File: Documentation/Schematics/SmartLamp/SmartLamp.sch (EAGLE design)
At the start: 25 parts, among them J1 POWER_JACKPTH_BREAD, Q1 IRLZ44Z, Q2 IRLZ44Z, Q3 IRLZ44Z, U1 HM-10, U2 DS3231MZ

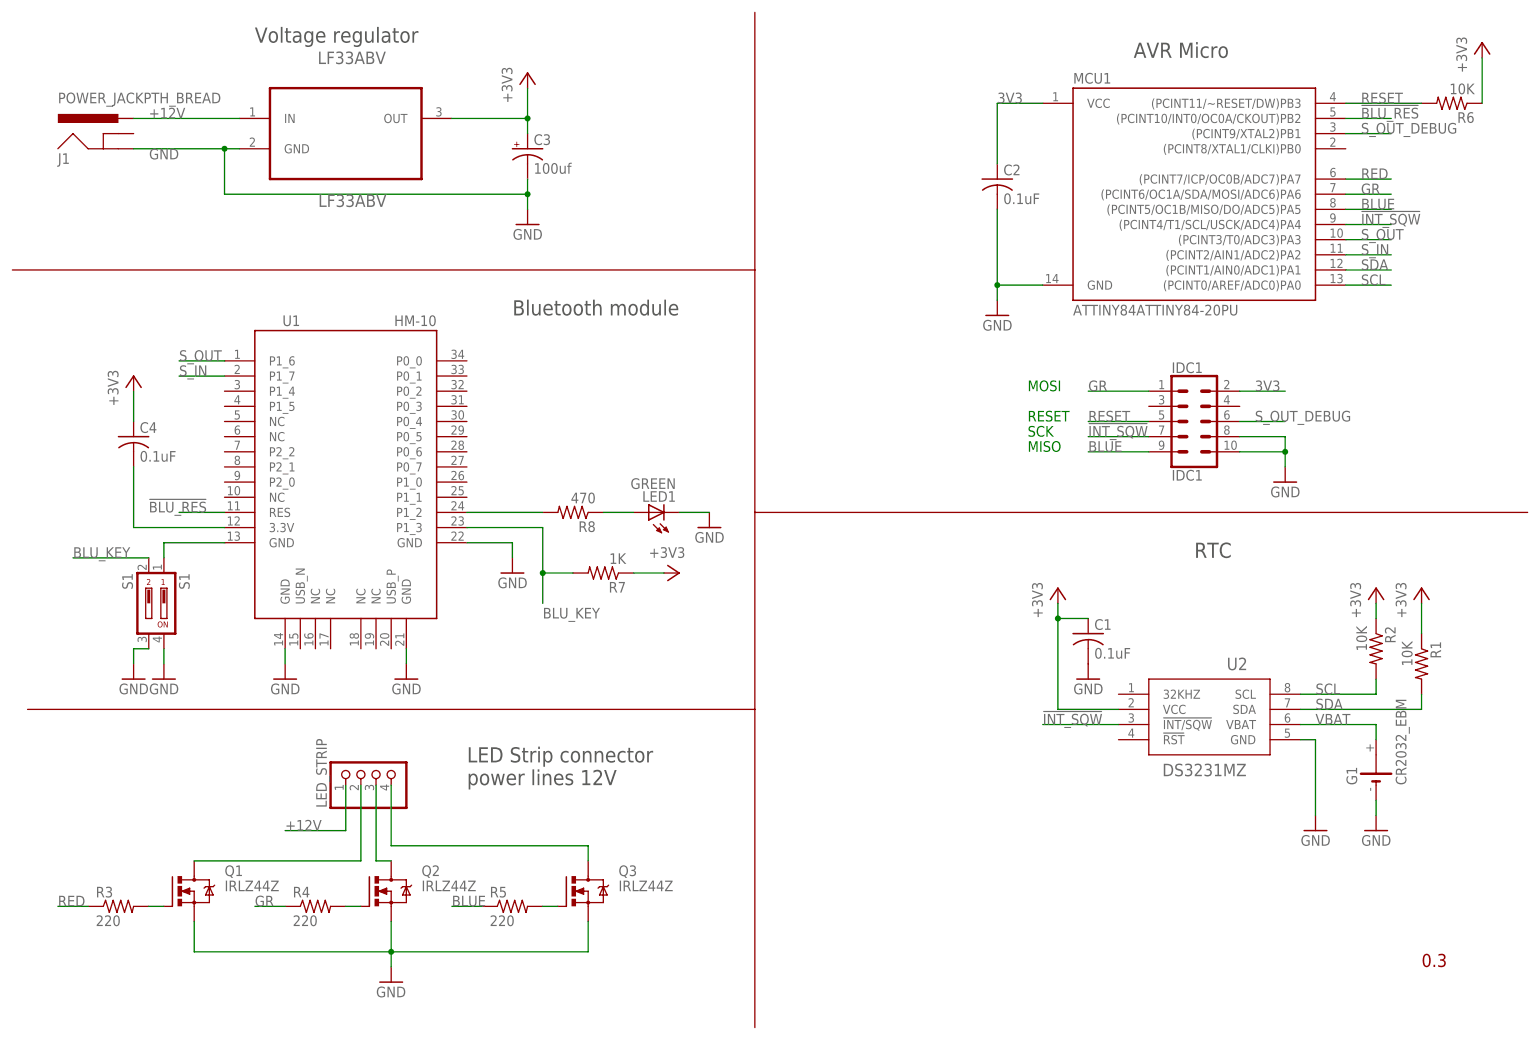
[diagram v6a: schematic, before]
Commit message: Fixed IO connections to micro, in schematic and main.cpp
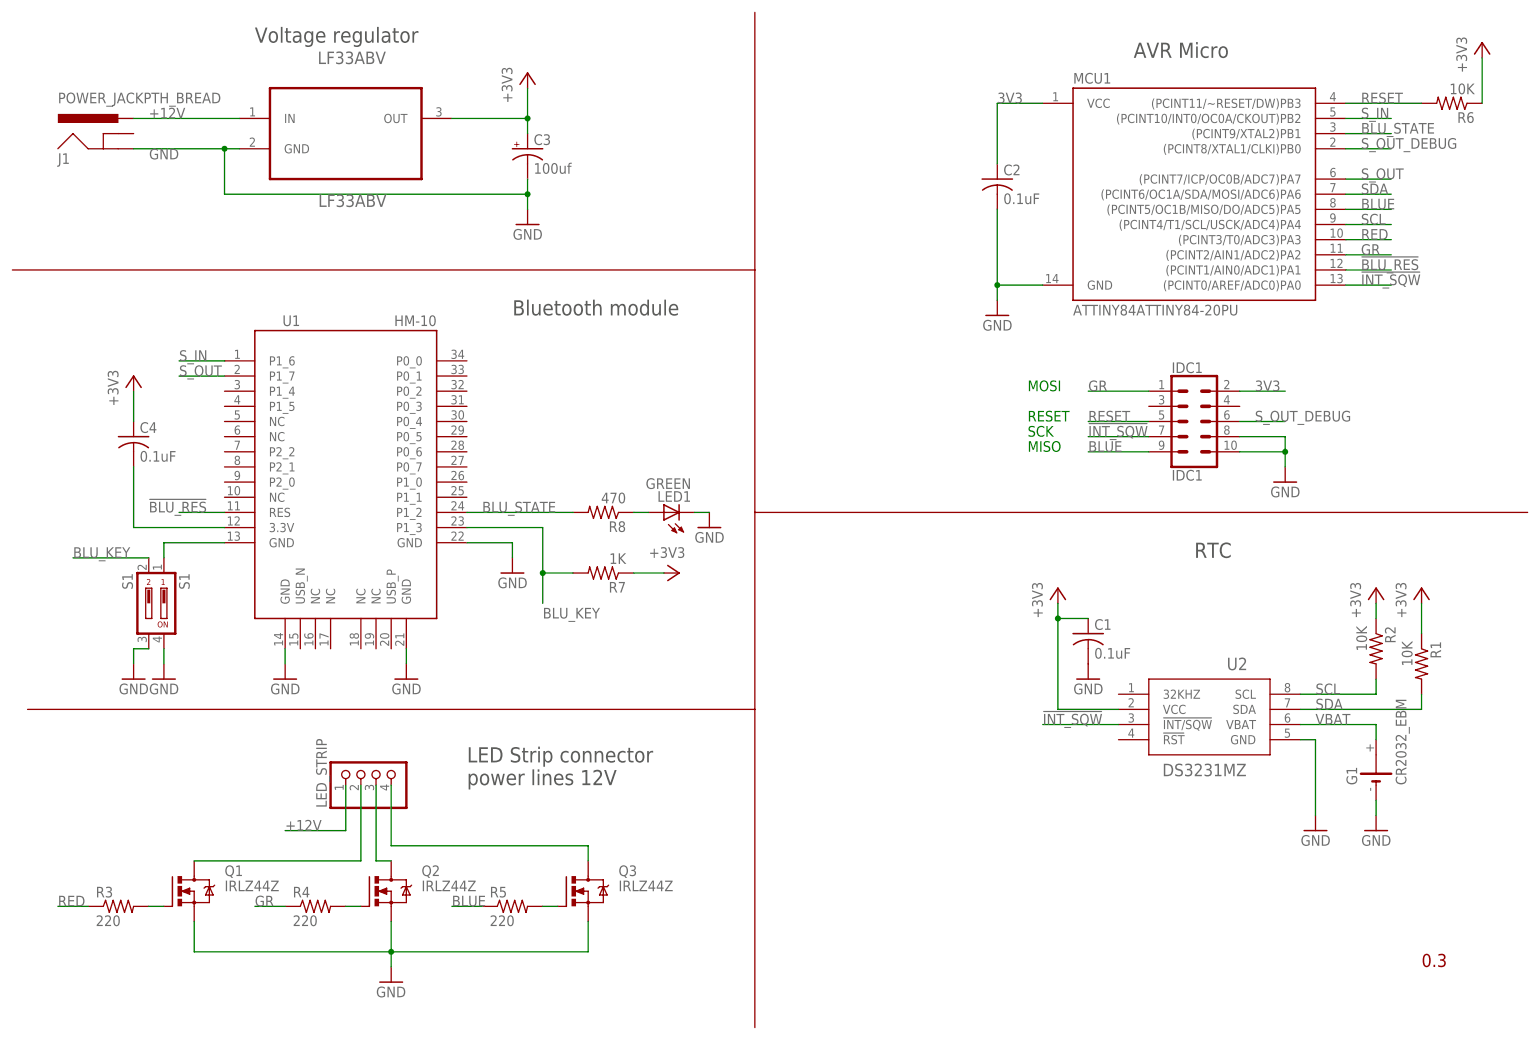
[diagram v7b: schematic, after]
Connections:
- removed net N$9: R8.2, U1.P1_2
- new net BLU_STATE: MCU1.(PCINT9/XTAL2)PB1, R8.2, U1.P1_2
- net !BLU_RES: now also MCU1.(PCINT1/AIN0/ADC1)PA1; no longer MCU1.(PCINT10/INT0/OC0A/CKOUT)PB2
- net !INT_SQW: now also MCU1.(PCINT0/AREF/ADC0)PA0; no longer MCU1.(PCINT4/T1/SCL/USCK/ADC4)PA4
- net GR: now also MCU1.(PCINT2/AIN1/ADC2)PA2; no longer MCU1.(PCINT6/OC1A/SDA/MOSI/ADC6)PA6
- net RED: now also MCU1.(PCINT3/T0/ADC3)PA3; no longer MCU1.(PCINT7/ICP/OC0B/ADC7)PA7
- net SCL: now also MCU1.(PCINT4/T1/SCL/USCK/ADC4)PA4; no longer MCU1.(PCINT0/AREF/ADC0)PA0
- net SDA: now also MCU1.(PCINT6/OC1A/SDA/MOSI/ADC6)PA6; no longer MCU1.(PCINT1/AIN0/ADC1)PA1
- net S_IN: now also MCU1.(PCINT10/INT0/OC0A/CKOUT)PB2, U1.P1_6; no longer MCU1.(PCINT2/AIN1/ADC2)PA2, U1.P1_7
- net S_OUT: now also MCU1.(PCINT7/ICP/OC0B/ADC7)PA7, U1.P1_7; no longer MCU1.(PCINT3/T0/ADC3)PA3, U1.P1_6
- net S_OUT_DEBUG: now also MCU1.(PCINT8/XTAL1/CLKI)PB0; no longer MCU1.(PCINT9/XTAL2)PB1
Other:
- moved on the sheet: LED1, R8
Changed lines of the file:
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@@
 <instance part="U1" gate="G$1" x="58.42" y="93.98"/>
 <instance part="R7" gate="G$1" x="101.6" y="81.28" rot="R180"/>
-<instance part="R8" gate="G$1" x="96.52" y="91.44" rot="R180"/>
-<instance part="LED1" gate="G$1" x="109.22" y="91.44" rot="R90"/>
+<instance part="R8" gate="G$1" x="101.6" y="91.44" rot="R180"/>
+<instance part="LED1" gate="G$1" x="111.76" y="91.44" rot="R90"/>
 <instance part="GND7" gate="1" x="27.94" y="63.5" rot="MR0"/>
 <instance part="GND8" gate="1" x="48.26" y="63.5" rot="MR0"/>
@@
 <segment>
 <pinref part="LED1" gate="G$1" pin="C"/>
-<wire x1="114.3" y1="91.44" x2="119.38" y2="91.44" width="0.1524" layer="91"/>
+<wire x1="116.84" y1="91.44" x2="119.38" y2="91.44" width="0.1524" layer="91"/>
 <pinref part="GND12" gate="1" pin="GND"/>
 </segment>
@@
 </segment>
 <segment>
-<pinref part="MCU1" gate="G$1" pin="(PCINT1/AIN0/ADC1)PA1"/>
-<wire x1="226.06" y1="132.08" x2="233.68" y2="132.08" width="0.1524" layer="91"/>
-<label x="228.6" y="132.08" size="1.778" layer="95"/>
+<pinref part="MCU1" gate="G$1" pin="(PCINT6/OC1A/SDA/MOSI/ADC6)PA6"/>
+<wire x1="226.06" y1="144.78" x2="233.68" y2="144.78" width="0.1524" layer="91"/>
+<label x="228.6" y="144.78" size="1.778" layer="95" font="vector"/>
 </segment>
 </net>
@@
 </segment>
 <segment>
-<pinref part="MCU1" gate="G$1" pin="(PCINT0/AREF/ADC0)PA0"/>
-<wire x1="226.06" y1="129.54" x2="233.68" y2="129.54" width="0.1524" layer="91"/>
-<label x="228.6" y="129.54" size="1.778" layer="95"/>
+<pinref part="MCU1" gate="G$1" pin="(PCINT4/T1/SCL/USCK/ADC4)PA4"/>
+<wire x1="226.06" y1="139.7" x2="233.68" y2="139.7" width="0.1524" layer="91"/>
+<label x="228.6" y="139.7" size="1.778" layer="95" font="vector"/>
 </segment>
 </net>
@@
 </segment>
 <segment>
-<pinref part="MCU1" gate="G$1" pin="(PCINT4/T1/SCL/USCK/ADC4)PA4"/>
-<wire x1="226.06" y1="139.7" x2="233.68" y2="139.7" width="0.1524" layer="91"/>
-<label x="228.6" y="139.7" size="1.778" layer="95" font="vector"/>
-</segment>
-<segment>
 <pinref part="IDC1" gate="G$1" pin="7"/>
 <wire x1="193.04" y1="104.14" x2="182.88" y2="104.14" width="0.1524" layer="91"/>
 <label x="182.88" y="104.14" size="1.778" layer="95" font="vector"/>
+</segment>
+<segment>
+<pinref part="MCU1" gate="G$1" pin="(PCINT0/AREF/ADC0)PA0"/>
+<wire x1="226.06" y1="129.54" x2="233.68" y2="129.54" width="0.1524" layer="91"/>
+<label x="228.6" y="129.54" size="1.778" layer="95" font="vector"/>
 </segment>
 </net>
@@
 <net name="S_OUT" class="0">
 <segment>
+<pinref part="MCU1" gate="G$1" pin="(PCINT7/ICP/OC0B/ADC7)PA7"/>
+<wire x1="226.06" y1="147.32" x2="233.68" y2="147.32" width="0.1524" layer="91"/>
+<label x="228.6" y="147.32" size="1.778" layer="95" font="vector"/>
+</segment>
+<segment>
+<pinref part="U1" gate="G$1" pin="P1_7"/>
+<wire x1="38.1" y1="114.3" x2="30.48" y2="114.3" width="0.1524" layer="91"/>
+<label x="30.48" y="114.3" size="1.778" layer="95" font="vector"/>
+</segment>
+</net>
+<net name="S_IN" class="0">
+<segment>
+<pinref part="MCU1" gate="G$1" pin="(PCINT10/INT0/OC0A/CKOUT)PB2"/>
+<wire x1="226.06" y1="157.48" x2="233.68" y2="157.48" width="0.1524" layer="91"/>
+<label x="228.6" y="157.48" size="1.778" layer="95" font="vector"/>
+</segment>
+<segment>
 <pinref part="U1" gate="G$1" pin="P1_6"/>
 <wire x1="38.1" y1="116.84" x2="30.48" y2="116.84" width="0.1524" layer="91"/>
-<label x="30.48" y="116.84" size="1.778" layer="95"/>
-</segment>
-<segment>
-<pinref part="MCU1" gate="G$1" pin="(PCINT3/T0/ADC3)PA3"/>
-<wire x1="226.06" y1="137.16" x2="233.68" y2="137.16" width="0.1524" layer="91"/>
-<label x="228.6" y="137.16" size="1.778" layer="95"/>
-</segment>
-</net>
-<net name="S_IN" class="0">
-<segment>
-<pinref part="U1" gate="G$1" pin="P1_7"/>
-<wire x1="38.1" y1="114.3" x2="30.48" y2="114.3" width="0.1524" layer="91"/>
-<label x="30.48" y="114.3" size="1.778" layer="95"/>
-</segment>
-<segment>
-<pinref part="MCU1" gate="G$1" pin="(PCINT2/AIN1/ADC2)PA2"/>
-<wire x1="226.06" y1="134.62" x2="233.68" y2="134.62" width="0.1524" layer="91"/>
-<label x="228.6" y="134.62" size="1.778" layer="95"/>
-</segment>
-</net>
-<net name="N$9" class="0">
+<label x="30.48" y="116.84" size="1.778" layer="95" font="vector"/>
+</segment>
+</net>
+<net name="BLU_STATE" class="0">
 <segment>
 <pinref part="U1" gate="G$1" pin="P1_2"/>
 <pinref part="R8" gate="G$1" pin="2"/>
-<wire x1="78.74" y1="91.44" x2="91.44" y2="91.44" width="0.1524" layer="91"/>
+<wire x1="78.74" y1="91.44" x2="96.52" y2="91.44" width="0.1524" layer="91"/>
+<label x="81.28" y="91.44" size="1.778" layer="95" font="vector"/>
+</segment>
+<segment>
+<pinref part="MCU1" gate="G$1" pin="(PCINT9/XTAL2)PB1"/>
+<wire x1="226.06" y1="154.94" x2="233.68" y2="154.94" width="0.1524" layer="91"/>
+<label x="228.6" y="154.94" size="1.778" layer="95" font="vector"/>
 </segment>
 </net>
@@
 <pinref part="R8" gate="G$1" pin="1"/>
 <pinref part="LED1" gate="G$1" pin="A"/>
-<wire x1="101.6" y1="91.44" x2="106.68" y2="91.44" width="0.1524" layer="91"/>
+<wire x1="109.22" y1="91.44" x2="106.68" y2="91.44" width="0.1524" layer="91"/>
 </segment>
 </net>
@@
 </segment>
 <segment>
-<pinref part="MCU1" gate="G$1" pin="(PCINT7/ICP/OC0B/ADC7)PA7"/>
-<wire x1="226.06" y1="147.32" x2="233.68" y2="147.32" width="0.1524" layer="91"/>
-<label x="228.6" y="147.32" size="1.778" layer="95"/>
+<pinref part="MCU1" gate="G$1" pin="(PCINT3/T0/ADC3)PA3"/>
+<wire x1="226.06" y1="137.16" x2="233.68" y2="137.16" width="0.1524" layer="91"/>
+<label x="228.6" y="137.16" size="1.778" layer="95" font="vector"/>
 </segment>
 </net>
@@
 </segment>
 <segment>
-<pinref part="MCU1" gate="G$1" pin="(PCINT6/OC1A/SDA/MOSI/ADC6)PA6"/>
-<wire x1="226.06" y1="144.78" x2="233.68" y2="144.78" width="0.1524" layer="91"/>
-<label x="228.6" y="144.78" size="1.778" layer="95"/>
-</segment>
-<segment>
 <pinref part="IDC1" gate="G$1" pin="1"/>
 <wire x1="193.04" y1="111.76" x2="182.88" y2="111.76" width="0.1524" layer="91"/>
 <label x="182.88" y="111.76" size="1.778" layer="95" font="vector"/>
 </segment>
+<segment>
+<pinref part="MCU1" gate="G$1" pin="(PCINT2/AIN1/ADC2)PA2"/>
+<wire x1="226.06" y1="134.62" x2="233.68" y2="134.62" width="0.1524" layer="91"/>
+<label x="228.6" y="134.62" size="1.778" layer="95" font="vector"/>
+</segment>
 </net>
 <net name="BLUE" class="0">
@@
 <net name="!BLU_RES" class="0">
 <segment>
-<pinref part="MCU1" gate="G$1" pin="(PCINT10/INT0/OC0A/CKOUT)PB2"/>
-<wire x1="226.06" y1="157.48" x2="233.68" y2="157.48" width="0.1524" layer="91"/>
-<label x="228.6" y="157.48" size="1.778" layer="95"/>
-</segment>
-<segment>
 <pinref part="U1" gate="G$1" pin="RES"/>
 <wire x1="38.1" y1="91.44" x2="30.48" y2="91.44" width="0.1524" layer="91"/>
 <label x="25.4" y="91.44" size="1.778" layer="95"/>
+</segment>
+<segment>
+<pinref part="MCU1" gate="G$1" pin="(PCINT1/AIN0/ADC1)PA1"/>
+<wire x1="226.06" y1="132.08" x2="233.68" y2="132.08" width="0.1524" layer="91"/>
+<label x="228.6" y="132.08" size="1.778" layer="95" font="vector"/>
 </segment>
 </net>
@@
 <net name="S_OUT_DEBUG" class="0">
 <segment>
-<pinref part="MCU1" gate="G$1" pin="(PCINT9/XTAL2)PB1"/>
-<wire x1="226.06" y1="154.94" x2="233.68" y2="154.94" width="0.1524" layer="91"/>
-<label x="228.6" y="154.94" size="1.778" layer="95" font="vector"/>
-</segment>
-<segment>
 <pinref part="IDC1" gate="G$1" pin="6"/>
 <wire x1="208.28" y1="106.68" x2="215.9" y2="106.68" width="0.1524" layer="91"/>
 <label x="210.82" y="106.68" size="1.778" layer="95" font="vector"/>
 </segment>
-</net>
+<segment>
+<pinref part="MCU1" gate="G$1" pin="(PCINT8/XTAL1/CLKI)PB0"/>
+<wire x1="226.06" y1="152.4" x2="233.68" y2="152.4" width="0.1524" layer="91"/>
+<label x="228.6" y="152.4" size="1.778" layer="95" font="vector"/>
+</segment>
+</net>

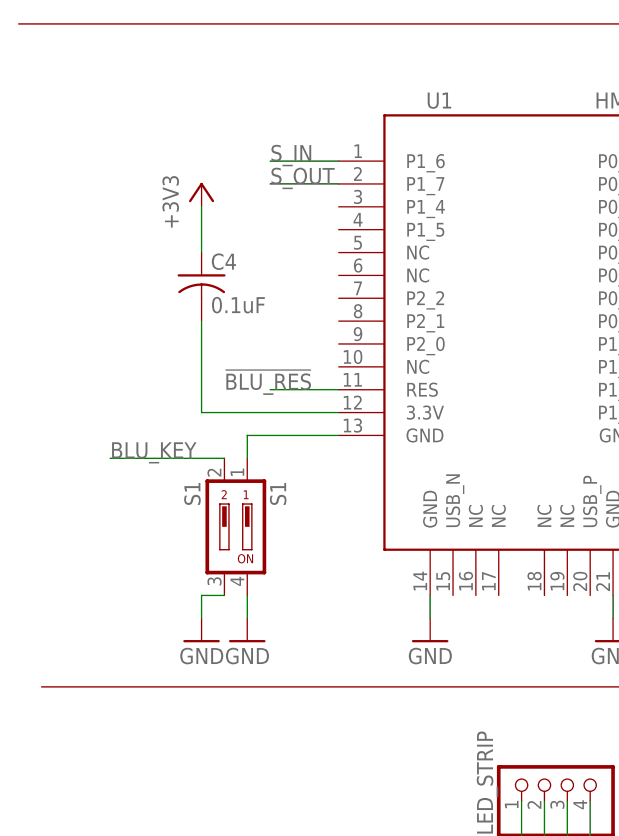
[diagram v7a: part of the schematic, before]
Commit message: Fixed cap on HM-10 module...
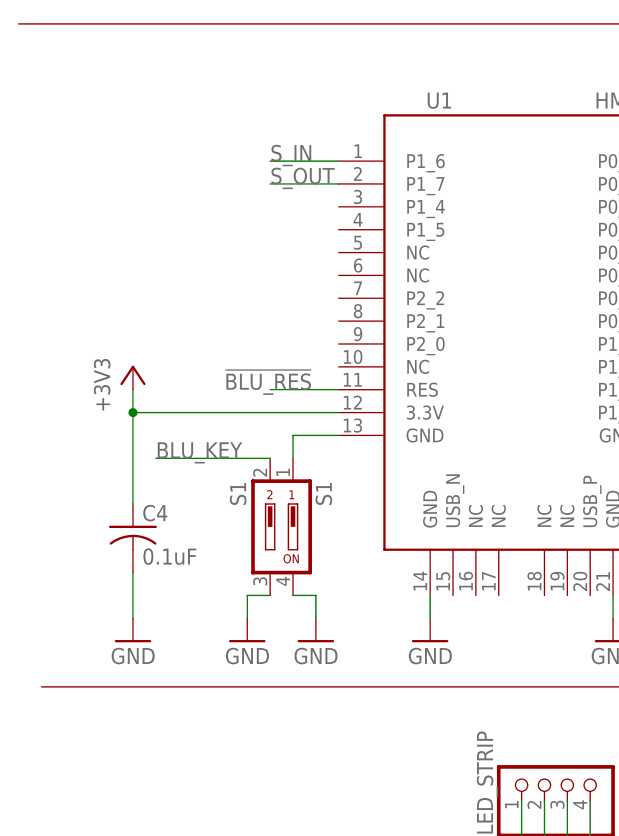
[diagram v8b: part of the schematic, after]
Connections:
- removed net N$1 (its old number): U1.3.3V
- net +3V3: now also U1.3.3V
- net GND: now also C4.2
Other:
- moved on the sheet: C4, S1
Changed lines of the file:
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@@
 <part name="Q2" library="transistor-power" deviceset="IRLZ44Z" device=""/>
 <part name="Q3" library="transistor-power" deviceset="IRLZ44Z" device=""/>
+<part name="GND3" library="supply1" deviceset="GND" device=""/>
 </parts>
 <sheets>
@@
 <instance part="R8" gate="G$1" x="101.6" y="91.44" rot="R180"/>
 <instance part="LED1" gate="G$1" x="111.76" y="91.44" rot="R90"/>
-<instance part="GND7" gate="1" x="27.94" y="63.5" rot="MR0"/>
+<instance part="GND7" gate="1" x="35.56" y="63.5" rot="MR0"/>
 <instance part="GND8" gate="1" x="48.26" y="63.5" rot="MR0"/>
 <instance part="GND9" gate="1" x="68.58" y="63.5" rot="MR0"/>
 <instance part="GND11" gate="1" x="86.36" y="81.28" rot="MR0"/>
 <instance part="GND12" gate="1" x="119.38" y="88.9" rot="MR0"/>
-<instance part="C4" gate="G$1" x="22.86" y="104.14"/>
+<instance part="C4" gate="G$1" x="15.24" y="76.2"/>
 <instance part="GND10" gate="1" x="66.04" y="12.7"/>
 <instance part="LED_STRIP" gate="A" x="63.5" y="48.26" rot="R90"/>
@@
 <instance part="FRAME1" gate="G$1" x="0" y="0"/>
 <instance part="GND13" gate="1" x="231.14" y="38.1" rot="MR0"/>
-<instance part="S1" gate="1" x="27.94" y="76.2" rot="R180"/>
+<instance part="S1" gate="1" x="33.02" y="76.2" rot="R180"/>
 <instance part="+3V1" gate="G$1" x="248.92" y="170.18"/>
 <instance part="+3V2" gate="G$1" x="177.8" y="78.74"/>
@@
 <instance part="+3V5" gate="G$1" x="88.9" y="165.1"/>
 <instance part="+3V6" gate="G$1" x="114.3" y="81.28" rot="R270"/>
-<instance part="+3V7" gate="G$1" x="22.86" y="114.3"/>
+<instance part="+3V7" gate="G$1" x="15.24" y="93.98"/>
 <instance part="GND5" gate="1" x="167.64" y="124.46" rot="MR0"/>
-<instance part="GND6" gate="1" x="22.86" y="63.5" rot="MR0"/>
+<instance part="GND6" gate="1" x="27.94" y="63.5" rot="MR0"/>
 <instance part="G1" gate="G$1" x="231.14" y="48.26" rot="R90"/>
 <instance part="U2" gate="A" x="203.2" y="58.42"/>
@@
 <instance part="Q2" gate="G$1" x="63.5" y="27.94"/>
 <instance part="Q3" gate="G$1" x="96.52" y="27.94"/>
+<instance part="GND3" gate="1" x="15.24" y="63.5" rot="MR0"/>
 </instances>
 <busses>
@@
 </segment>
 <segment>
+<pinref part="C4" gate="G$1" pin="2"/>
+<pinref part="GND3" gate="1" pin="GND"/>
+<wire x1="15.24" y1="71.12" x2="15.24" y2="66.04" width="0.1524" layer="91"/>
+</segment>
+<segment>
+<pinref part="GND7" gate="1" pin="GND"/>
+<pinref part="S1" gate="1" pin="4"/>
+<wire x1="35.56" y1="66.04" x2="35.56" y2="68.58" width="0.1524" layer="91"/>
+<wire x1="35.56" y1="68.58" x2="33.02" y2="68.58" width="0.1524" layer="91"/>
+</segment>
+<segment>
+<pinref part="GND6" gate="1" pin="GND"/>
 <pinref part="S1" gate="1" pin="3"/>
-<wire x1="25.4" y1="68.58" x2="22.86" y2="68.58" width="0.1524" layer="91"/>
-<wire x1="22.86" y1="68.58" x2="22.86" y2="66.04" width="0.1524" layer="91"/>
-<pinref part="GND6" gate="1" pin="GND"/>
-</segment>
-<segment>
-<pinref part="S1" gate="1" pin="4"/>
-<pinref part="GND7" gate="1" pin="GND"/>
-<wire x1="27.94" y1="68.58" x2="27.94" y2="66.04" width="0.1524" layer="91"/>
+<wire x1="27.94" y1="66.04" x2="27.94" y2="68.58" width="0.1524" layer="91"/>
+<wire x1="27.94" y1="68.58" x2="30.48" y2="68.58" width="0.1524" layer="91"/>
 </segment>
 </net>
@@
 <segment>
 <pinref part="S1" gate="1" pin="2"/>
-<wire x1="25.4" y1="83.82" x2="12.7" y2="83.82" width="0.1524" layer="91"/>
-<label x="12.7" y="83.82" size="1.778" layer="95" font="vector"/>
+<wire x1="30.48" y1="83.82" x2="17.78" y2="83.82" width="0.1524" layer="91"/>
+<label x="17.78" y="83.82" size="1.778" layer="95" font="vector"/>
 </segment>
 </net>
@@
 <wire x1="226.06" y1="152.4" x2="233.68" y2="152.4" width="0.1524" layer="91"/>
 <label x="228.6" y="152.4" size="1.778" layer="95" font="vector"/>
-</segment>
-</net>
-<net name="N$1" class="0">
-<segment>
-<pinref part="U1" gate="G$1" pin="3.3V"/>
-<wire x1="38.1" y1="88.9" x2="22.86" y2="88.9" width="0.1524" layer="91"/>
-<wire x1="22.86" y1="88.9" x2="22.86" y2="99.06" width="0.1524" layer="91"/>
 </segment>
 </net>
@@
 <pinref part="C4" gate="G$1" pin="1"/>
 <pinref part="+3V7" gate="G$1" pin="+3V3"/>
-<wire x1="22.86" y1="106.68" x2="22.86" y2="111.76" width="0.1524" layer="91"/>
-</segment>
-</net>
-<net name="N$2" class="0">
-<segment>
+<wire x1="15.24" y1="78.74" x2="15.24" y2="88.9" width="0.1524" layer="91"/>
+<pinref part="U1" gate="G$1" pin="3.3V"/>
+<wire x1="15.24" y1="88.9" x2="15.24" y2="91.44" width="0.1524" layer="91"/>
+<wire x1="38.1" y1="88.9" x2="15.24" y2="88.9" width="0.1524" layer="91"/>
+<junction x="15.24" y="88.9"/>
+</segment>
+</net>
+<net name="N$1" class="0">
+<segment>
+<pinref part="S1" gate="1" pin="1"/>
+<wire x1="33.02" y1="83.82" x2="33.02" y2="86.36" width="0.1524" layer="91"/>
 <pinref part="U1" gate="G$1" pin="GND@1"/>
-<wire x1="27.94" y1="86.36" x2="38.1" y2="86.36" width="0.1524" layer="91"/>
-<pinref part="S1" gate="1" pin="1"/>
-<wire x1="27.94" y1="86.36" x2="27.94" y2="83.82" width="0.1524" layer="91"/>
-</segment>
-</net>
+<wire x1="33.02" y1="86.36" x2="38.1" y2="86.36" width="0.1524" layer="91"/>
+</segment>
+</net>
